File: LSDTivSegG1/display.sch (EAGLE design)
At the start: 94 parts, among them IC1 MEGA8-P, IC2 MAX232, IC3 PCF8574P, IC4 PCF8574P, IC5 PCF8574P, IC6 PCF8574P

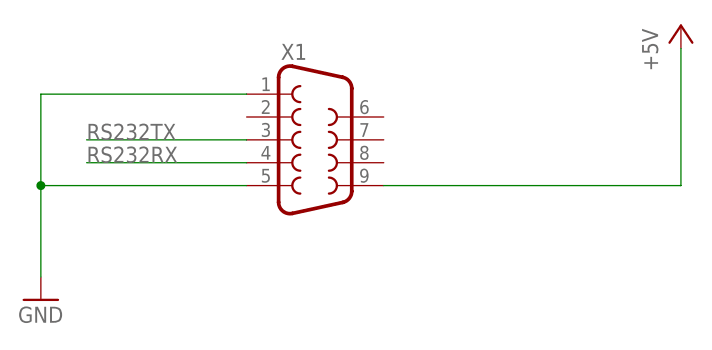
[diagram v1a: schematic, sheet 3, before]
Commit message: added jumper to interrupt VCC via RS232 to debug
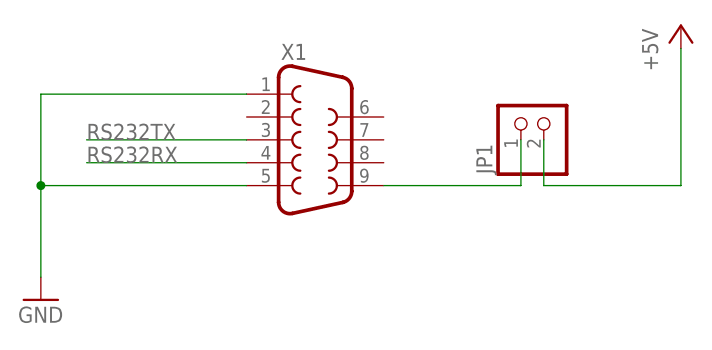
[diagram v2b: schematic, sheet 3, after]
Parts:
- added JP1: (no value), pinhead:PINHD-1X2
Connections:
- new net N$48: JP1.1, X1.9
- net +5V: now also JP1.2; no longer X1.9
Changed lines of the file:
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@@
 <part name="FRAME6" library="frames" library_urn="urn:adsk.eagle:library:229" deviceset="A4L-LOC" device=""/>
 <part name="FRAME7" library="frames" library_urn="urn:adsk.eagle:library:229" deviceset="A4P-LOC" device=""/>
+<part name="JP1" library="pinhead" library_urn="urn:adsk.eagle:library:325" deviceset="PINHD-1X2" device="" package3d_urn="urn:adsk.eagle:package:22435/2"/>
 </parts>
 <sheets>
@@
 <instance part="P+3" gate="1" x="71.12" y="0"/>
 <instance part="FRAME3" gate="G$1" x="-88.9" y="-101.6"/>
+<instance part="JP1" gate="G$1" x="55.88" y="-10.16" rot="R90"/>
 </instances>
 <busses>
@@
 <net name="+5V" class="0">
 <segment>
-<pinref part="X1" gate="G$1" pin="9"/>
-<wire x1="38.1" y1="-17.78" x2="71.12" y2="-17.78" width="0.1524" layer="91"/>
 <pinref part="P+3" gate="1" pin="+5V"/>
 <wire x1="71.12" y1="-17.78" x2="71.12" y2="-2.54" width="0.1524" layer="91"/>
-</segment>
-</net>
+<pinref part="JP1" gate="G$1" pin="2"/>
+<wire x1="55.88" y1="-12.7" x2="55.88" y2="-17.78" width="0.1524" layer="91"/>
+<wire x1="55.88" y1="-17.78" x2="71.12" y2="-17.78" width="0.1524" layer="91"/>
+</segment>
+</net>
+<net name="N$48" class="0">
+<segment>
+<pinref part="X1" gate="G$1" pin="9"/>
+<pinref part="JP1" gate="G$1" pin="1"/>
+<wire x1="38.1" y1="-17.78" x2="53.34" y2="-17.78" width="0.1524" layer="91"/>
+<wire x1="53.34" y1="-17.78" x2="53.34" y2="-12.7" width="0.1524" layer="91"/>
+</segment>
+</net>

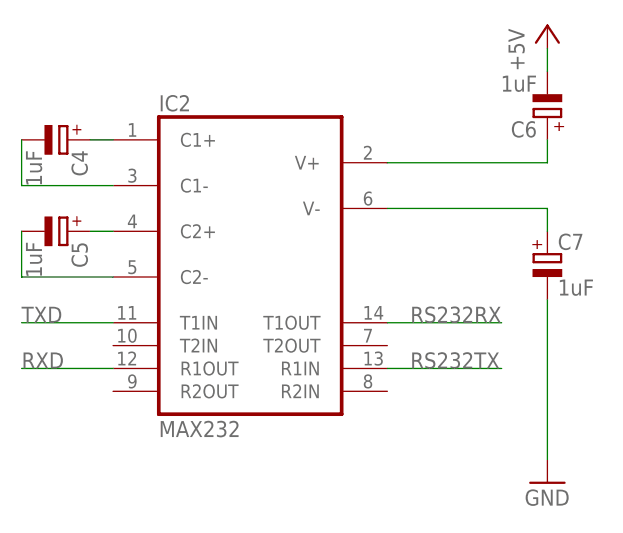
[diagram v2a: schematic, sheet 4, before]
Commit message: added jumper to rs232 connector to interrupt 5V supply
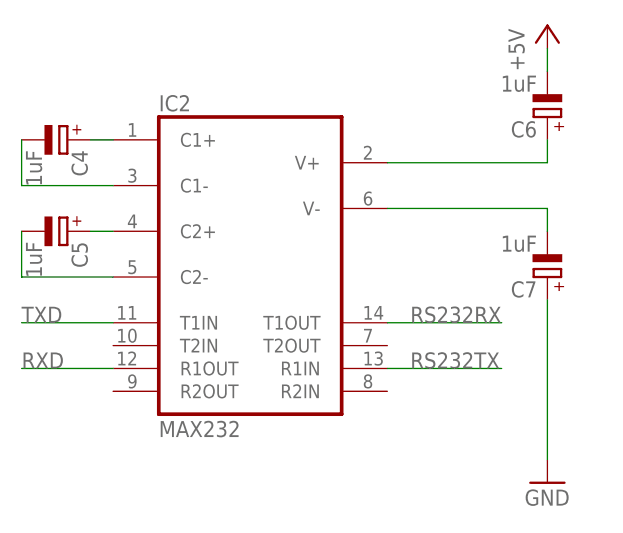
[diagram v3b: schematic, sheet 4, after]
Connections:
- net GND: now also C7.+; no longer C7.-
- net N$8: now also C7.-; no longer C7.+
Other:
- moved on the sheet: C7
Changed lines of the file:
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@@
 <instance part="C5" gate="G$1" x="-10.16" y="20.32" rot="R270"/>
 <instance part="C6" gate="G$1" x="43.18" y="33.02" rot="R180"/>
-<instance part="C7" gate="G$1" x="43.18" y="17.78"/>
+<instance part="C7" gate="G$1" x="43.18" y="15.24" rot="R180"/>
 <instance part="FRAME4" gate="G$1" x="-114.3" y="-76.2"/>
 </instances>
@@
 </segment>
 </net>
-<net name="N$8" class="0">
-<segment>
-<pinref part="IC2" gate="G$1" pin="V-"/>
-<pinref part="C7" gate="G$1" pin="+"/>
-<wire x1="25.4" y1="22.86" x2="43.18" y2="22.86" width="0.1524" layer="91"/>
-<wire x1="43.18" y1="22.86" x2="43.18" y2="20.32" width="0.1524" layer="91"/>
-</segment>
-</net>
-<net name="GND" class="0">
-<segment>
-<pinref part="C7" gate="G$1" pin="-"/>
-<pinref part="GND5" gate="1" pin="GND"/>
-<wire x1="43.18" y1="12.7" x2="43.18" y2="-5.08" width="0.1524" layer="91"/>
-</segment>
-</net>
 <net name="RS232RX" class="0">
 <segment>
@@
 </segment>
 </net>
+<net name="N$8" class="0">
+<segment>
+<pinref part="IC2" gate="G$1" pin="V-"/>
+<wire x1="25.4" y1="22.86" x2="43.18" y2="22.86" width="0.1524" layer="91"/>
+<pinref part="C7" gate="G$1" pin="-"/>
+<wire x1="43.18" y1="22.86" x2="43.18" y2="20.32" width="0.1524" layer="91"/>
+</segment>
+</net>
+<net name="GND" class="0">
+<segment>
+<pinref part="C7" gate="G$1" pin="+"/>
+<pinref part="GND5" gate="1" pin="GND"/>
+<wire x1="43.18" y1="12.7" x2="43.18" y2="-5.08" width="0.1524" layer="91"/>
+</segment>
+</net>

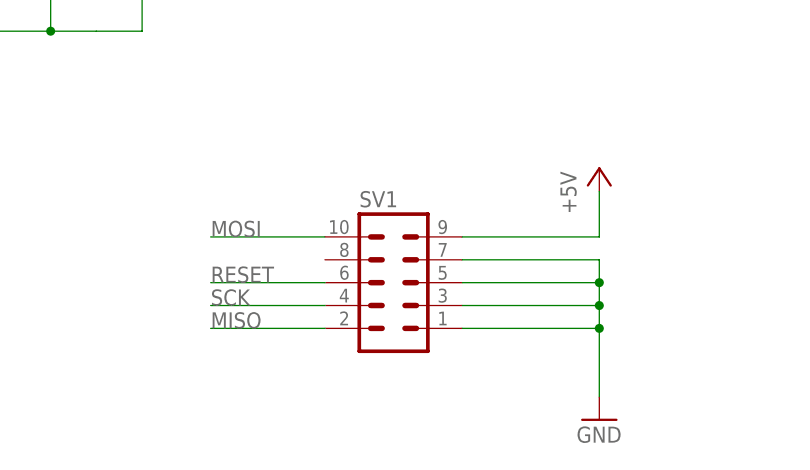
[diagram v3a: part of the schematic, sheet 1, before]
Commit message: fixed mirrored isp connector in display board
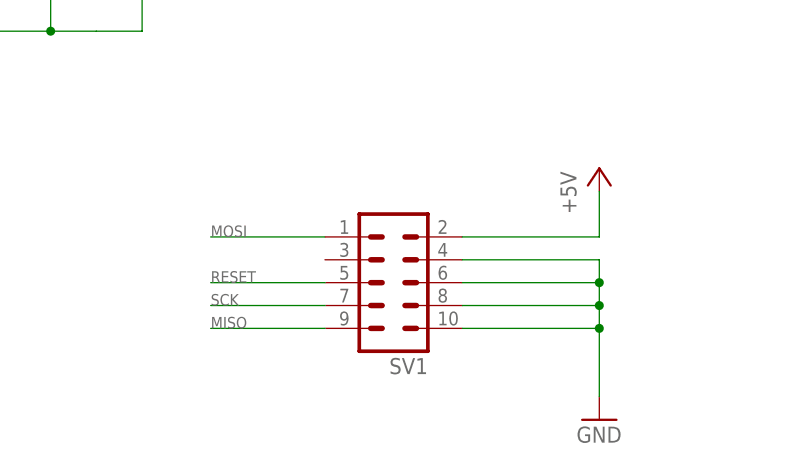
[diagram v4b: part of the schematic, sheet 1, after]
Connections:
- net +5V: now also SV1.2; no longer SV1.9
- net GND: now also SV1.10, SV1.4, SV1.6, SV1.8; no longer SV1.1, SV1.3, SV1.5, SV1.7
- net MISO: now also SV1.9; no longer SV1.2
- net MOSI: now also SV1.1; no longer SV1.10
- net RESET: now also SV1.5; no longer SV1.6
- net SCK: now also SV1.7; no longer SV1.4
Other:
- moved on the sheet: SV1
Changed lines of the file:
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@@
 <instance part="C2" gate="G$1" x="5.08" y="10.16"/>
 <instance part="C3" gate="G$1" x="-5.08" y="10.16"/>
-<instance part="SV1" gate="G$1" x="33.02" y="-40.64"/>
+<instance part="SV1" gate="G$1" x="33.02" y="-40.64" smashed="yes" rot="R180">
+<attribute name="VALUE" x="36.83" y="-30.48" size="1.778" layer="96" rot="R180"/>
+<attribute name="NAME" x="36.83" y="-49.022" size="1.778" layer="95" rot="R180"/>
+</instance>
 <instance part="P+2" gate="1" x="55.88" y="-27.94"/>
 <instance part="GND3" gate="1" x="55.88" y="-55.88"/>
@@
 </segment>
 <segment>
-<pinref part="SV1" gate="G$1" pin="6"/>
+<pinref part="SV1" gate="G$1" pin="5"/>
 <wire x1="25.4" y1="-40.64" x2="12.7" y2="-40.64" width="0.1524" layer="91"/>
-<label x="12.7" y="-40.64" size="1.778" layer="95"/>
+<label x="12.7" y="-40.64" size="1.27" layer="95"/>
 </segment>
 </net>
@@
 </segment>
 <segment>
-<pinref part="SV1" gate="G$1" pin="9"/>
 <pinref part="P+2" gate="1" pin="+5V"/>
+<wire x1="55.88" y1="-35.56" x2="55.88" y2="-30.48" width="0.1524" layer="91"/>
+<pinref part="SV1" gate="G$1" pin="2"/>
 <wire x1="40.64" y1="-35.56" x2="55.88" y2="-35.56" width="0.1524" layer="91"/>
-<wire x1="55.88" y1="-35.56" x2="55.88" y2="-30.48" width="0.1524" layer="91"/>
 </segment>
 <segment>
@@
 </segment>
 <segment>
-<pinref part="SV1" gate="G$1" pin="7"/>
 <pinref part="GND3" gate="1" pin="GND"/>
-<wire x1="40.64" y1="-38.1" x2="55.88" y2="-38.1" width="0.1524" layer="91"/>
 <wire x1="55.88" y1="-38.1" x2="55.88" y2="-40.64" width="0.1524" layer="91"/>
-<pinref part="SV1" gate="G$1" pin="5"/>
 <wire x1="55.88" y1="-40.64" x2="55.88" y2="-43.18" width="0.1524" layer="91"/>
 <wire x1="55.88" y1="-43.18" x2="55.88" y2="-45.72" width="0.1524" layer="91"/>
 <wire x1="55.88" y1="-45.72" x2="55.88" y2="-53.34" width="0.1524" layer="91"/>
+<pinref part="SV1" gate="G$1" pin="4"/>
+<wire x1="55.88" y1="-38.1" x2="40.64" y2="-38.1" width="0.1524" layer="91"/>
+<pinref part="SV1" gate="G$1" pin="6"/>
 <wire x1="40.64" y1="-40.64" x2="55.88" y2="-40.64" width="0.1524" layer="91"/>
 <junction x="55.88" y="-40.64"/>
-<pinref part="SV1" gate="G$1" pin="3"/>
+<pinref part="SV1" gate="G$1" pin="8"/>
 <wire x1="40.64" y1="-43.18" x2="55.88" y2="-43.18" width="0.1524" layer="91"/>
 <junction x="55.88" y="-43.18"/>
-<pinref part="SV1" gate="G$1" pin="1"/>
+<pinref part="SV1" gate="G$1" pin="10"/>
 <wire x1="40.64" y1="-45.72" x2="55.88" y2="-45.72" width="0.1524" layer="91"/>
 <junction x="55.88" y="-45.72"/>
@@
 </segment>
 <segment>
-<pinref part="SV1" gate="G$1" pin="4"/>
+<pinref part="SV1" gate="G$1" pin="7"/>
 <wire x1="25.4" y1="-43.18" x2="12.7" y2="-43.18" width="0.1524" layer="91"/>
-<label x="12.7" y="-43.18" size="1.778" layer="95"/>
+<label x="12.7" y="-43.18" size="1.27" layer="95"/>
 </segment>
 </net>
@@
 </segment>
 <segment>
-<pinref part="SV1" gate="G$1" pin="2"/>
+<pinref part="SV1" gate="G$1" pin="9"/>
 <wire x1="25.4" y1="-45.72" x2="12.7" y2="-45.72" width="0.1524" layer="91"/>
-<label x="12.7" y="-45.72" size="1.778" layer="95"/>
+<label x="12.7" y="-45.72" size="1.27" layer="95"/>
 </segment>
 </net>
@@
 </segment>
 <segment>
-<pinref part="SV1" gate="G$1" pin="10"/>
+<pinref part="SV1" gate="G$1" pin="1"/>
 <wire x1="25.4" y1="-35.56" x2="12.7" y2="-35.56" width="0.1524" layer="91"/>
-<label x="12.7" y="-35.56" size="1.778" layer="95"/>
-</segment>
-</net>
+<label x="12.7" y="-35.56" size="1.27" layer="95"/>
+</segment>
+</net>
